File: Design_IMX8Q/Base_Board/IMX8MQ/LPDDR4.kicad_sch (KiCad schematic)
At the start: 4 parts, among them U1 MIMX8MQ6CVAHZAB, U2 IS43LQ32256A-062BLI

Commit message: changes vias pad size
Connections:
- net WIFI/BLE_RTS: now reaches U1.B4 (ECSPI1_MISO)
- net WIFI/BLE_CTS: now reaches U1.D4 (ECSPI1_SS0)
- net ENET_MDIO: now reaches U1.N19 (ENET_MDIO)
- net ENET_MDC: now reaches U1.N20 (ENET_MDC)
- net ENET_TX_CL: now reaches U1.P19 (ENET_TX_CTL)
- net ENET_TD3: now reaches U1.P20 (ENET_TD3)
- net ENET_TXC: now reaches U1.T19 (ENET_TXC)
- net ENET_RXC: now reaches U1.T20 (ENET_RXC)
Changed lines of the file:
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@@
+    (stroke (width 0) (type default))
+  )
+  (wire (pts (xy 129.54 140.97) (xy 140.97 140.97))
     (stroke (width 0) (type default))
   )
@@
     (stroke (width 0) (type default))
   )
+  (wire (pts (xy 129.54 161.29) (xy 146.05 161.29))
+    (stroke (width 0) (type default))
+  )
   (wire (pts (xy 53.34 120.65) (xy 46.99 120.65))
     (stroke (width 0) (type default))
@@
     (stroke (width 0) (type default))
   )
+  (wire (pts (xy 129.54 158.75) (xy 146.05 158.75))
+    (stroke (width 0) (type default))
+  )
   (wire (pts (xy 246.38 97.79) (xy 252.73 97.79))
     (stroke (width 0) (type default))
@@
     (stroke (width 0) (type default))
   )
+  (wire (pts (xy 129.54 156.21) (xy 146.05 156.21))
+    (stroke (width 0) (type default))
+  )
   (wire (pts (xy 205.74 90.17) (xy 199.39 90.17))
     (stroke (width 0) (type default))
@@
     (stroke (width 0) (type default))
   )
+  (wire (pts (xy 129.54 151.13) (xy 146.05 151.13))
+    (stroke (width 0) (type default))
+  )
   (wire (pts (xy 129.54 85.09) (xy 135.89 85.09))
     (stroke (width 0) (type default))
@@
     (stroke (width 0) (type default))
   )
+  (wire (pts (xy 129.54 153.67) (xy 146.05 153.67))
+    (stroke (width 0) (type default))
+  )
   (wire (pts (xy 246.38 105.41) (xy 252.73 105.41))
     (stroke (width 0) (type default))
@@
     (stroke (width 0) (type default))
   )
+  (wire (pts (xy 129.54 163.83) (xy 146.05 163.83))
+    (stroke (width 0) (type default))
+  )
   (wire (pts (xy 350.52 95.25) (xy 356.87 95.25))
     (stroke (width 0) (type default))
@@
   )
   (wire (pts (xy 358.14 52.07) (xy 358.14 54.61))
+    (stroke (width 0) (type default))
+  )
+  (wire (pts (xy 129.54 133.35) (xy 140.97 133.35))
     (stroke (width 0) (type default))
   )
@@
     )
   )
+  (global_label "ENET_TX_CL" (shape input) (at 146.05 156.21 0) (fields_autoplaced)
+    (effects (font (size 1 1)) (justify left))
+    (property "Intersheetrefs" "${INTERSHEET_REFS}" (at 157.0046 156.21 0)
+      (effects (font (size 1.27 1.27)) (justify left) hide)
+    )
+  )
   (global_label "DRAM_DATA2_A" (shape input) (at 199.39 90.17 180) (fields_autoplaced)
     (effects (font (size 1.27 1.27)) (justify right))
@@
     (property "Intersheetrefs" "${INTERSHEET_REFS}" (at 291.7947 82.55 0)
       (effects (font (size 1.27 1.27)) (justify right) hide)
+    )
+  )
+  (global_label "ENET_RXC" (shape input) (at 146.05 161.29 0) (fields_autoplaced)
+    (effects (font (size 1 1)) (justify left))
+    (property "Intersheetrefs" "${INTERSHEET_REFS}" (at 155.6713 161.29 0)
+      (effects (font (size 1.27 1.27)) (justify left) hide)
     )
   )
@@
     )
   )
+  (global_label "ENET_TXC" (shape input) (at 146.05 158.75 0) (fields_autoplaced)
+    (effects (font (size 1 1)) (justify left))
+    (property "Intersheetrefs" "${INTERSHEET_REFS}" (at 155.4332 158.75 0)
+      (effects (font (size 1.27 1.27)) (justify left) hide)
+    )
+  )
   (global_label "CA1_A" (shape input) (at 199.39 59.69 180) (fields_autoplaced)
     (effects (font (size 1.27 1.27)) (justify right))
@@
     )
   )
+  (global_label "WIFI{slash}BLE_RTS" (shape input) (at 140.97 133.35 0) (fields_autoplaced)
+    (effects (font (size 1.27 1.27)) (justify left))
+    (property "Intersheetrefs" "${INTERSHEET_REFS}" (at 156.8177 133.35 0)
+      (effects (font (size 1.27 1.27)) (justify left) hide)
+    )
+  )
   (global_label "DRAM_DATA3_A" (shape input) (at 135.89 85.09 0) (fields_autoplaced)
     (effects (font (size 1.27 1.27)) (justify left))
@@
     (property "Intersheetrefs" "${INTERSHEET_REFS}" (at 35.2547 77.47 0)
       (effects (font (size 1.27 1.27)) (justify right) hide)
+    )
+  )
+  (global_label "WIFI{slash}BLE_CTS" (shape input) (at 140.97 140.97 0) (fields_autoplaced)
+    (effects (font (size 1.27 1.27)) (justify left))
+    (property "Intersheetrefs" "${INTERSHEET_REFS}" (at 156.8177 140.97 0)
+      (effects (font (size 1.27 1.27)) (justify left) hide)
     )
   )
@@
     )
   )
+  (global_label "ENET_MDC" (shape input) (at 146.05 153.67 0) (fields_autoplaced)
+    (effects (font (size 1 1)) (justify left))
+    (property "Intersheetrefs" "${INTERSHEET_REFS}" (at 155.8618 153.67 0)
+      (effects (font (size 1.27 1.27)) (justify left) hide)
+    )
+  )
   (global_label "CA3_B" (shape input) (at 303.53 67.31 180) (fields_autoplaced)
     (effects (font (size 1.27 1.27)) (justify right))
@@
     )
   )
+  (global_label "ENET_TD3" (shape input) (at 146.05 163.83 0) (fields_autoplaced)
+    (effects (font (size 1 1)) (justify left))
+    (property "Intersheetrefs" "${INTERSHEET_REFS}" (at 155.4332 163.83 0)
+      (effects (font (size 1.27 1.27)) (justify left) hide)
+    )
+  )
   (global_label "DQS1_B+" (shape input) (at 356.87 82.55 0) (fields_autoplaced)
     (effects (font (size 1.27 1.27)) (justify left))
@@
       (effects (font (size 1.27 1.27)) (justify left) hide)
     )
+  )
+  (global_label "ENET_MDIO" (shape input) (at 146.05 151.13 0) (fields_autoplaced)
+    (effects (font (size 1 1)) (justify left))
+    (property "Intersheetrefs" "${INTERSHEET_REFS}" (at 156.3856 151.13 0)
+      (effects (font (size 1.27 1.27)) (justify left) hide)
+    )

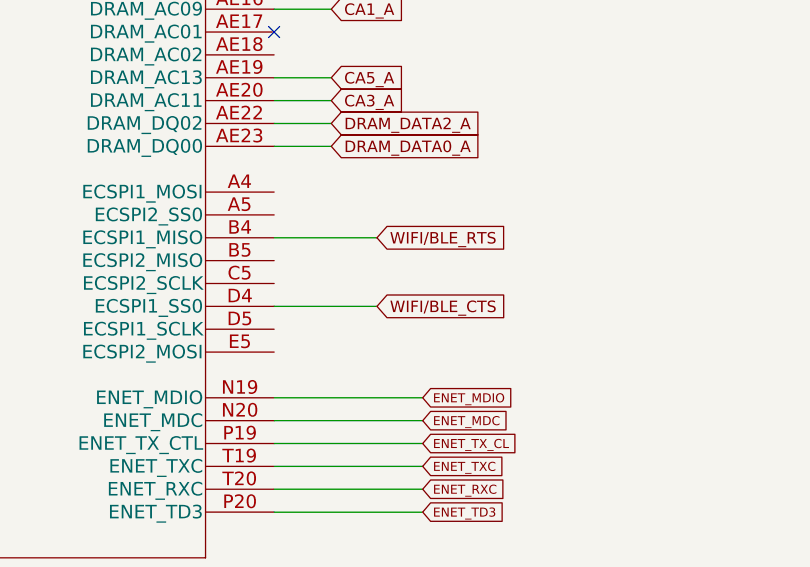
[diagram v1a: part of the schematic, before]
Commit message: Add QSPI and more color
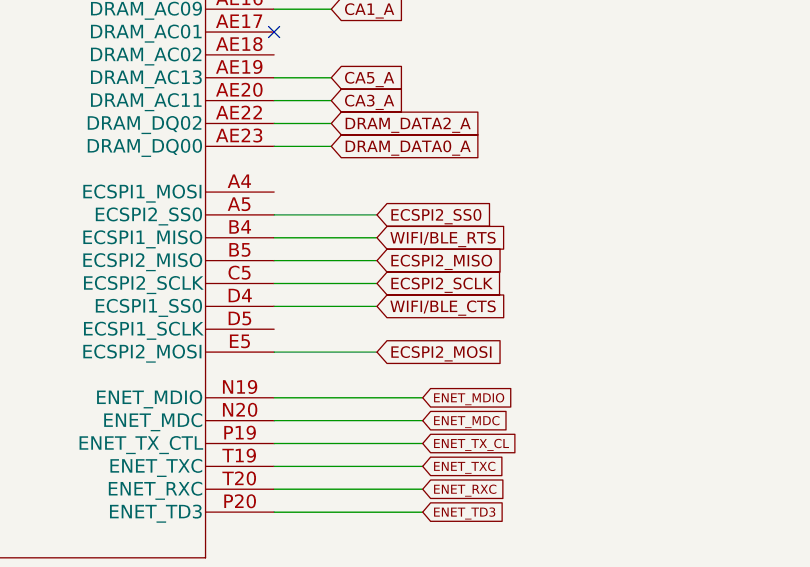
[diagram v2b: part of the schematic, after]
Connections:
- net ECSPI2_SS0: now reaches U1.A5 (ECSPI2_SS0)
- net ECSPI2_MISO: now reaches U1.B5 (ECSPI2_MISO)
- net ECSPI2_SCLK: now reaches U1.C5 (ECSPI2_SCLK)
- net ECSPI2_MOSI: now reaches U1.E5 (ECSPI2_MOSI)
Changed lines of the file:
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@@
+    (stroke (width 0) (type default))
+  )
+  (wire (pts (xy 129.54 130.81) (xy 140.97 130.81))
     (stroke (width 0) (type default))
   )
@@
     (stroke (width 0) (type default))
   )
+  (wire (pts (xy 129.54 146.05) (xy 140.97 146.05))
+    (stroke (width 0) (type default))
+  )
   (wire (pts (xy 246.38 95.25) (xy 252.73 95.25))
     (stroke (width 0) (type default))
@@
     (stroke (width 0) (type default))
   )
+  (wire (pts (xy 129.54 135.89) (xy 140.97 135.89))
+    (stroke (width 0) (type default))
+  )
   (wire (pts (xy 309.88 67.31) (xy 303.53 67.31))
     (stroke (width 0) (type default))
@@
   )
   (wire (pts (xy 309.88 72.39) (xy 303.53 72.39))
+    (stroke (width 0) (type default))
+  )
+  (wire (pts (xy 129.54 138.43) (xy 140.97 138.43))
     (stroke (width 0) (type default))
   )
@@
     )
   )
+  (global_label "ECSPI2_SCLK" (shape input) (at 140.97 138.43 0) (fields_autoplaced)
+    (effects (font (size 1.27 1.27)) (justify left))
+    (property "Intersheetrefs" "${INTERSHEET_REFS}" (at 156.3338 138.43 0)
+      (effects (font (size 1.27 1.27)) (justify left) hide)
+    )
+  )
   (global_label "CK_A+" (shape input) (at 199.39 44.45 180) (fields_autoplaced)
     (effects (font (size 1.27 1.27)) (justify right))
@@
     )
   )
+  (global_label "ECSPI2_SS0" (shape input) (at 140.97 130.81 0) (fields_autoplaced)
+    (effects (font (size 1.27 1.27)) (justify left))
+    (property "Intersheetrefs" "${INTERSHEET_REFS}" (at 155.1847 130.81 0)
+      (effects (font (size 1.27 1.27)) (justify left) hide)
+    )
+  )
   (global_label "CA2_A" (shape input) (at 135.89 82.55 0) (fields_autoplaced)
     (effects (font (size 1.27 1.27)) (justify left))
@@
     (property "Intersheetrefs" "${INTERSHEET_REFS}" (at 294.8185 62.23 0)
       (effects (font (size 1.27 1.27)) (justify right) hide)
+    )
+  )
+  (global_label "ECSPI2_MOSI" (shape input) (at 140.97 146.05 0) (fields_autoplaced)
+    (effects (font (size 1.27 1.27)) (justify left))
+    (property "Intersheetrefs" "${INTERSHEET_REFS}" (at 156.1524 146.05 0)
+      (effects (font (size 1.27 1.27)) (justify left) hide)
     )
   )
@@
       (effects (font (size 1.27 1.27)) (justify left) hide)
     )
+  )
+  (global_label "ECSPI2_MISO" (shape input) (at 140.97 135.89 0) (fields_autoplaced)
+    (effects (font (size 1.27 1.27)) (justify left))
+    (property "Intersheetrefs" "${INTERSHEET_REFS}" (at 156.1524 135.89 0)
+      (effects (font (size 1.27 1.27)) (justify left) hide)
+    )

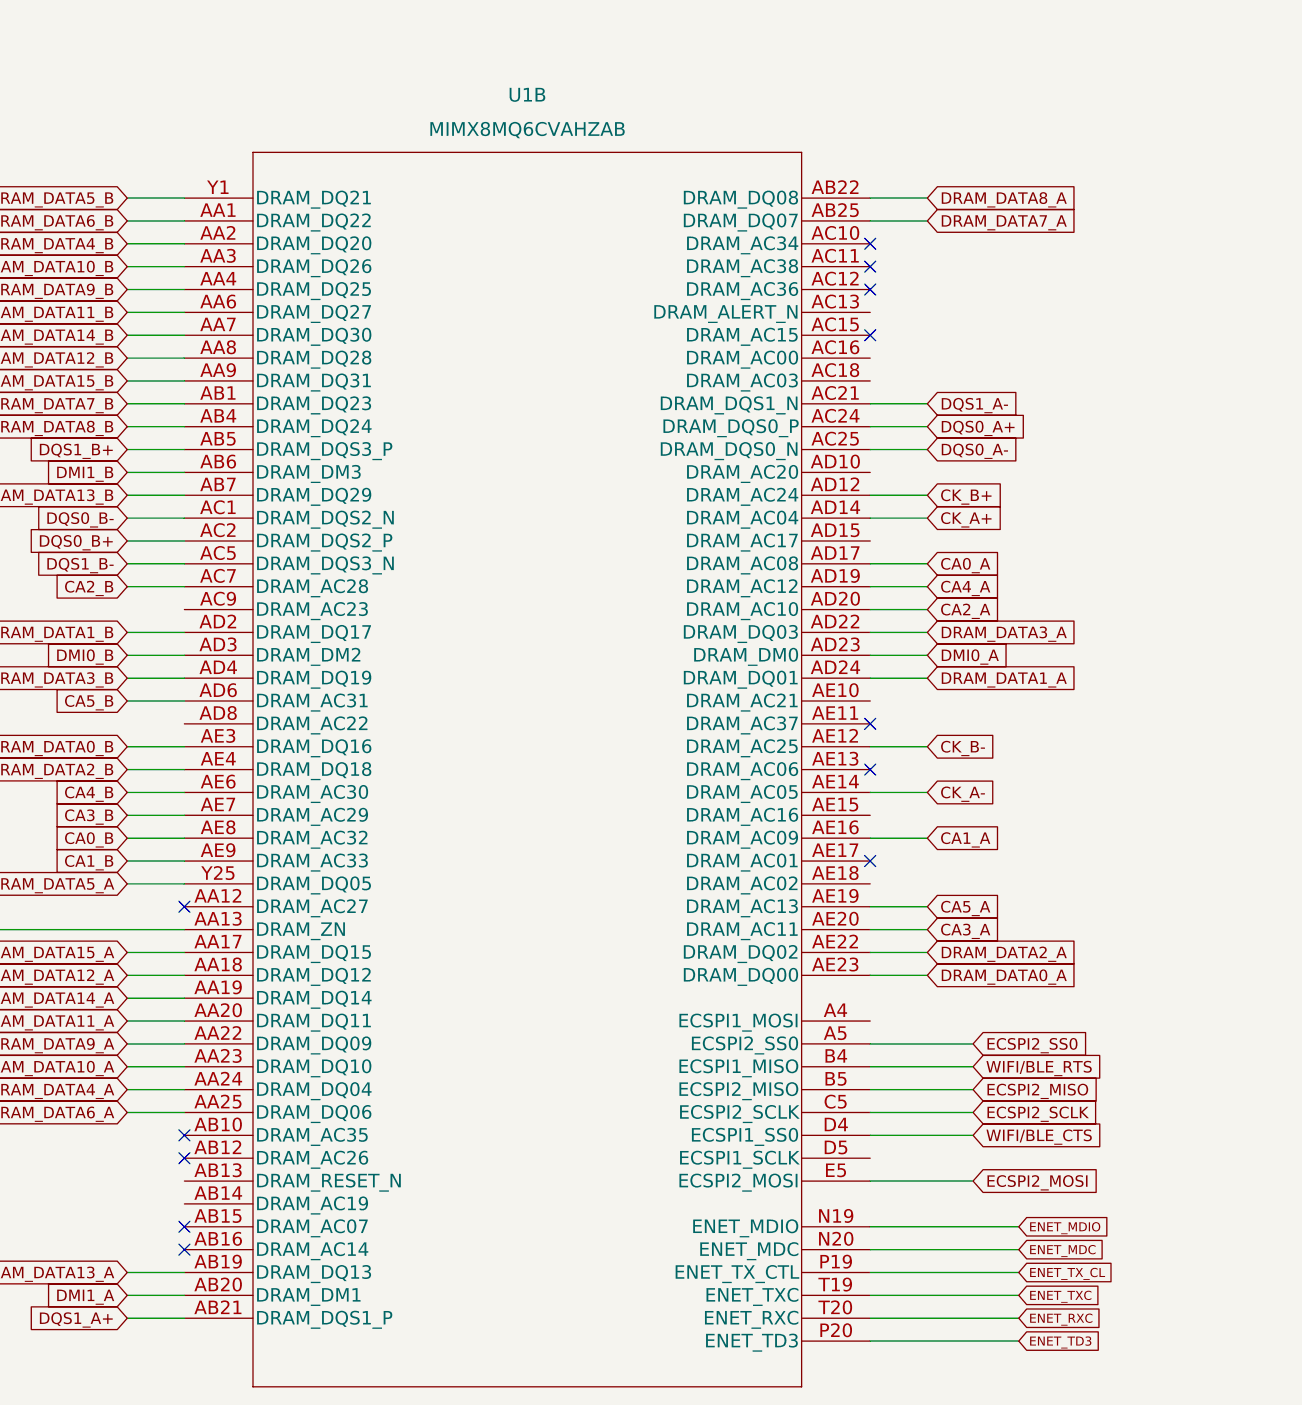
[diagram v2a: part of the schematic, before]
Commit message: it was inserted power control system
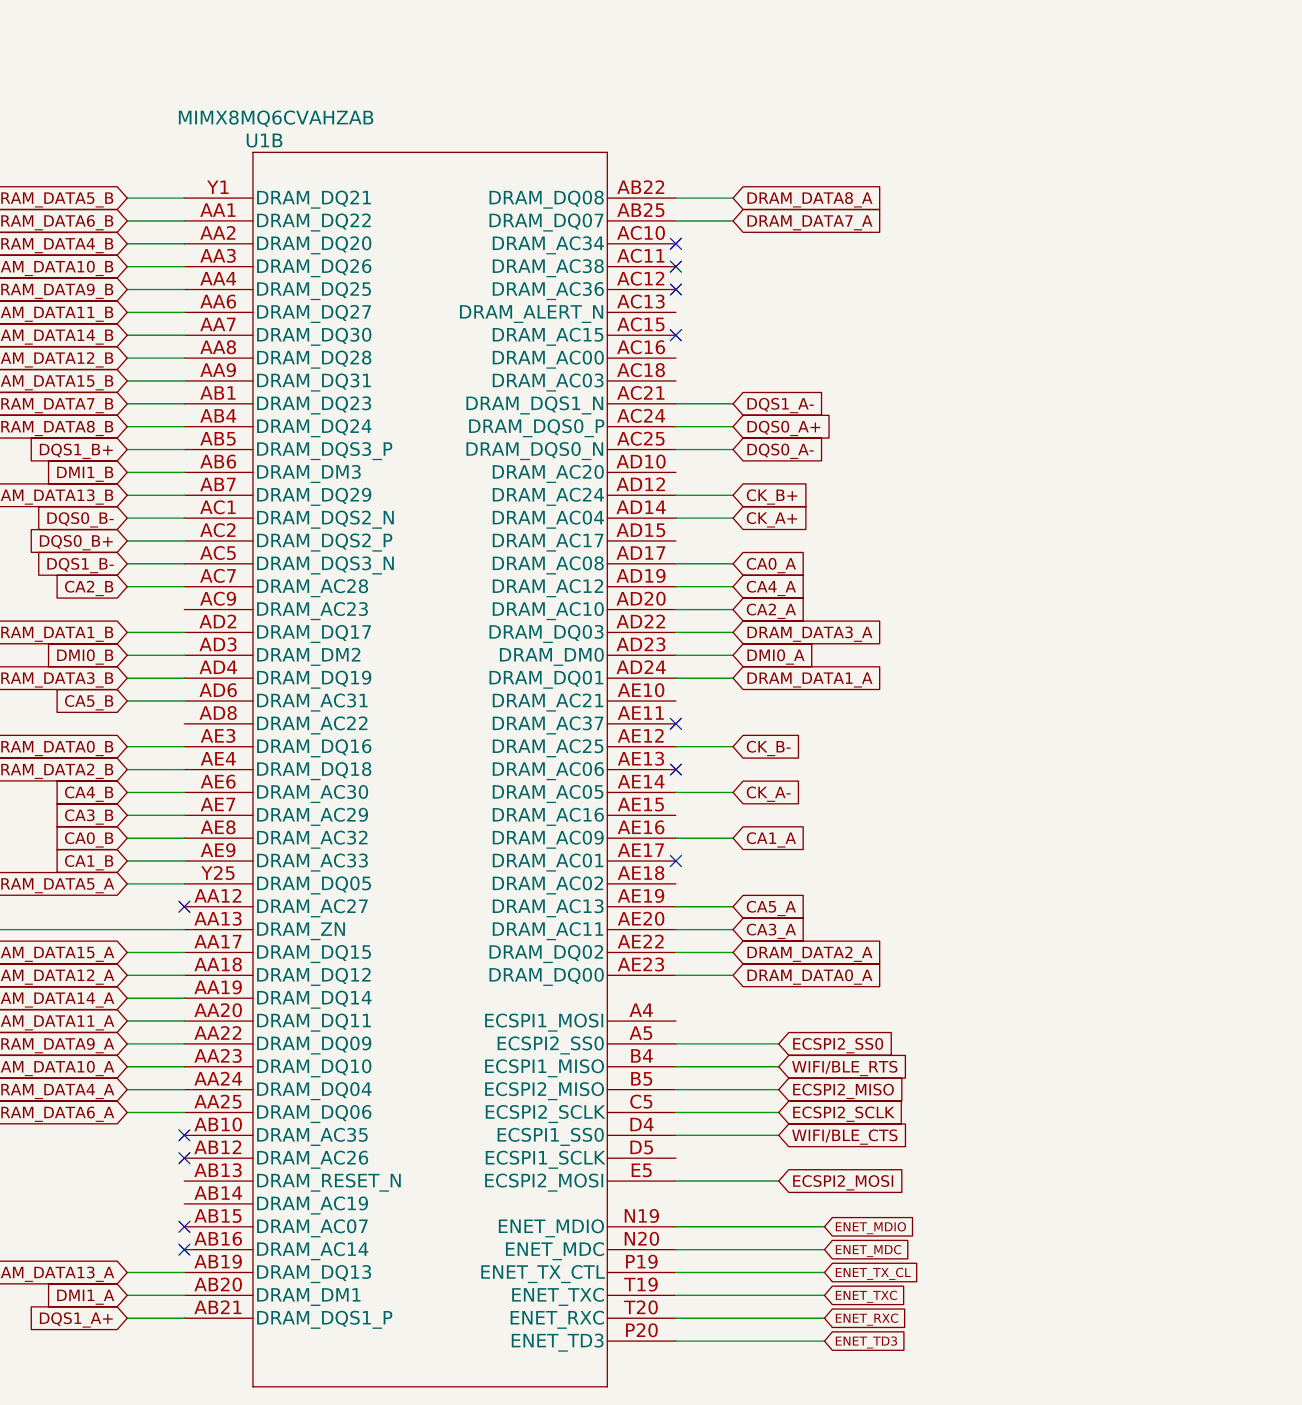
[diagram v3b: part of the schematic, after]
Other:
- moved on the sheet: U1B
